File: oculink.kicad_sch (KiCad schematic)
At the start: 14 parts, among them J1 OCuLink_x4_Amphenol_G14A42121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

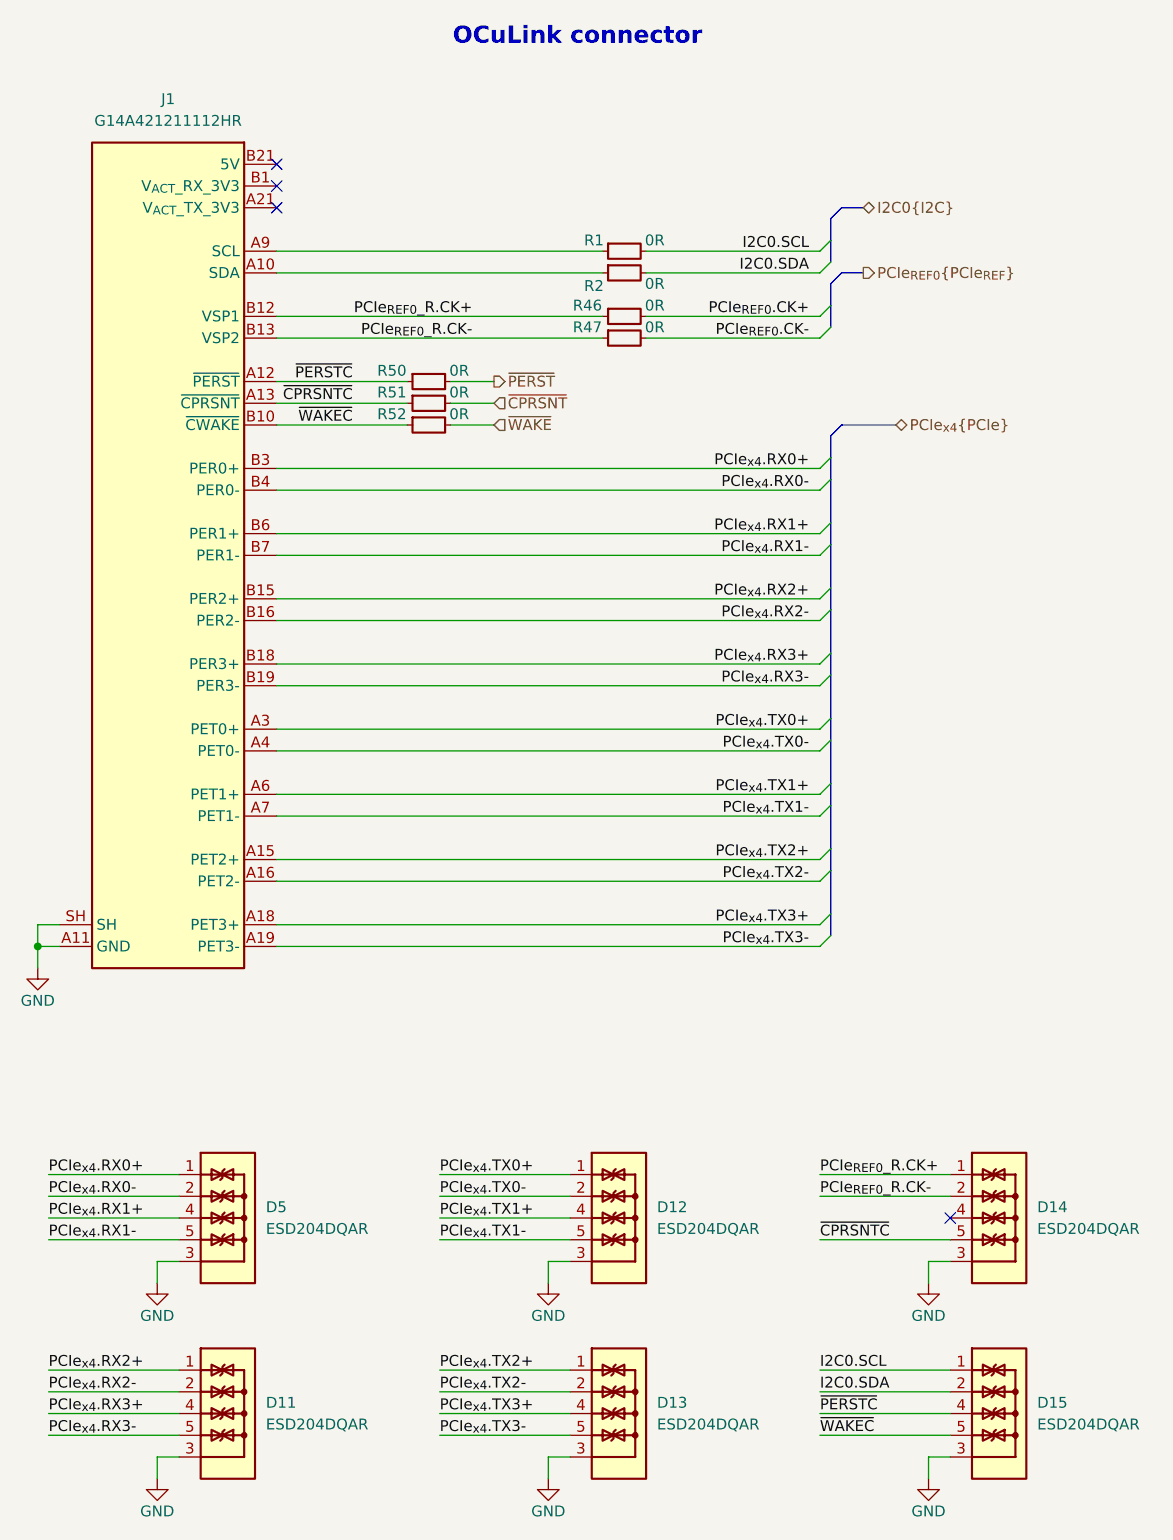
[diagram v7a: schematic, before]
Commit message: [#79262] Route high speed and power
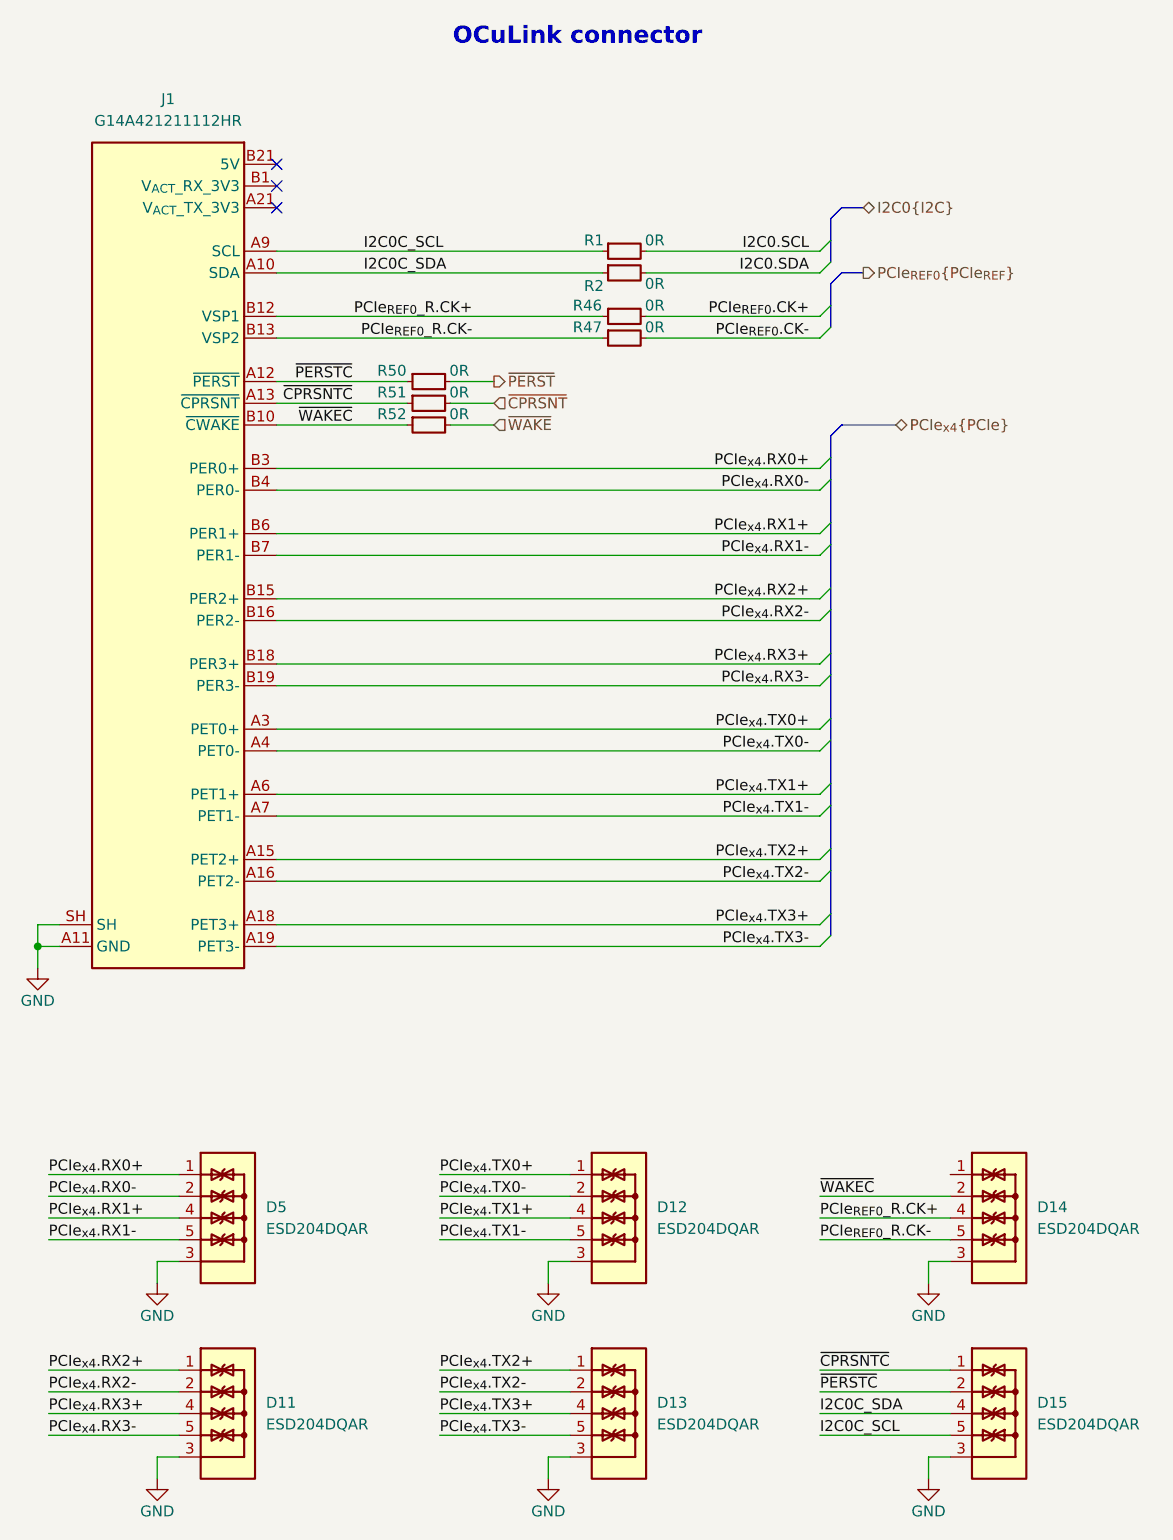
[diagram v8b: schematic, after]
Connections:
- net I2C0.SCL: no longer D15.1, D15.10
- net I2C0.SDA: no longer D15.2, D15.9
- net PCIe_{REF0}_R.CK+: now also D14.4, D14.7; no longer D14.1, D14.10
- net PCIe_{REF0}_R.CK-: now also D14.5, D14.6; no longer D14.2, D14.9
- net ~{CPRSNTC}: now also D15.1, D15.10; no longer D14.5, D14.6
- net ~{PERSTC}: now also D15.2, D15.9; no longer D15.4, D15.7
- net ~{WAKEC}: now also D14.2, D14.9; no longer D15.5, D15.6
- net I2C0C_SDA: now reaches J1.A10 (SDA), R2.1
- net I2C0C_SDA: now also D15.4, D15.7
- net I2C0C_SCL: now reaches J1.A9 (SCL), R1.1
- net I2C0C_SCL: now also D15.5, D15.6
- new net: D14.1, D14.10
- no-connect marks 4 -> 3
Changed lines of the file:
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@@
-	)
-	(no_connect
-		(at 246.38 215.9)
 	)
 	(no_connect
@@
 	(wire
 		(pts
+			(xy 231.14 213.36) (xy 246.38 213.36)
+		)
+		(stroke
+			(width 0)
+			(type default)
+		)
+	)
+	(wire
+		(pts
 			(xy 231.14 241.3) (xy 246.38 241.3)
 		)
@@
 	(wire
 		(pts
-			(xy 231.14 210.82) (xy 246.38 210.82)
+			(xy 231.14 215.9) (xy 246.38 215.9)
 		)
 		(stroke
@@
 	(wire
 		(pts
+			(xy 142.24 181.61) (xy 139.7 181.61)
+		)
+		(stroke
+			(width 0)
+			(type default)
+		)
+	)
+	(wire
+		(pts
+			(xy 231.14 173.99) (xy 167.64 173.99)
+		)
+		(stroke
+			(width 0)
+			(type default)
+		)
+	)
+	(wire
+		(pts
+			(xy 140.97 238.76) (xy 156.21 238.76)
+		)
+		(stroke
+			(width 0)
+			(type default)
+		)
+	)
+	(bus
+		(pts
+			(xy 232.41 152.4) (xy 232.41 157.48)
+		)
+		(stroke
+			(width 0)
+			(type default)
+		)
+	)
+	(wire
+		(pts
+			(xy 167.64 138.43) (xy 231.14 138.43)
+		)
+		(stroke
+			(width 0)
+			(type default)
+		)
+	)
+	(wire
+		(pts
+			(xy 153.67 220.98) (xy 153.67 223.52)
+		)
+		(stroke
+			(width 0)
+			(type default)
+		)
+	)
+	(wire
+		(pts
+			(xy 167.64 102.87) (xy 205.74 102.87)
+		)
+		(stroke
+			(width 0)
+			(type default)
+		)
+	)
+	(wire
+		(pts
+			(xy 199.39 220.98) (xy 201.93 220.98)
+		)
+		(stroke
+			(width 0)
+			(type default)
+		)
+	)
+	(wire
+		(pts
+			(xy 210.82 102.87) (xy 231.14 102.87)
+		)
+		(stroke
+			(width 0)
+			(type default)
+		)
+	)
+	(wire
+		(pts
 			(xy 231.14 218.44) (xy 246.38 218.44)
-		)
-		(stroke
-			(width 0)
-			(type default)
-		)
-	)
-	(wire
-		(pts
-			(xy 142.24 181.61) (xy 139.7 181.61)
-		)
-		(stroke
-			(width 0)
-			(type default)
-		)
-	)
-	(wire
-		(pts
-			(xy 231.14 173.99) (xy 167.64 173.99)
-		)
-		(stroke
-			(width 0)
-			(type default)
-		)
-	)
-	(wire
-		(pts
-			(xy 140.97 238.76) (xy 156.21 238.76)
-		)
-		(stroke
-			(width 0)
-			(type default)
-		)
-	)
-	(bus
-		(pts
-			(xy 232.41 152.4) (xy 232.41 157.48)
-		)
-		(stroke
-			(width 0)
-			(type default)
-		)
-	)
-	(wire
-		(pts
-			(xy 167.64 138.43) (xy 231.14 138.43)
-		)
-		(stroke
-			(width 0)
-			(type default)
-		)
-	)
-	(wire
-		(pts
-			(xy 153.67 220.98) (xy 153.67 223.52)
-		)
-		(stroke
-			(width 0)
-			(type default)
-		)
-	)
-	(wire
-		(pts
-			(xy 167.64 102.87) (xy 205.74 102.87)
-		)
-		(stroke
-			(width 0)
-			(type default)
-		)
-	)
-	(wire
-		(pts
-			(xy 199.39 220.98) (xy 201.93 220.98)
-		)
-		(stroke
-			(width 0)
-			(type default)
-		)
-	)
-	(wire
-		(pts
-			(xy 210.82 102.87) (xy 231.14 102.87)
-		)
-		(stroke
-			(width 0)
-			(type default)
-		)
-	)
-	(wire
-		(pts
-			(xy 231.14 213.36) (xy 246.38 213.36)
 		)
 		(stroke
@@
 	)
 	(label "~{CPRSNTC}"
-		(at 231.14 218.44 0)
+		(at 231.14 233.68 0)
 		(effects
 			(font
@@
 		)
 	)
-	(label "I2C0.SCL"
-		(at 231.14 233.68 0)
-		(effects
-			(font
-				(size 1.27 1.27)
-			)
-			(justify left bottom)
-		)
-	)
 	(label "PCIe_{REF0}_R.CK+"
 		(at 190.5 110.49 180)
@@
 		)
 	)
+	(label "I2C0C_SDA"
+		(at 231.14 238.76 0)
+		(effects
+			(font
+				(size 1.27 1.27)
+			)
+			(justify left bottom)
+		)
+	)
 	(label "PCIe_{x4}.RX1-"
 		(at 229.87 138.43 180)
@@
 		)
 	)
-	(label "~{WAKEC}"
-		(at 231.14 241.3 0)
-		(effects
-			(font
-				(size 1.27 1.27)
-			)
-			(justify left bottom)
-		)
-	)
 	(label "PCIe_{REF0}_R.CK+"
-		(at 231.14 210.82 0)
+		(at 231.14 215.9 0)
 		(effects
 			(font
@@
 	)
 	(label "~{PERSTC}"
-		(at 231.14 238.76 0)
+		(at 231.14 236.22 0)
 		(effects
 			(font
@@
 		)
 	)
-	(label "I2C0.SDA"
-		(at 231.14 236.22 0)
+	(label "I2C0C_SCL"
+		(at 177.8 102.87 0)
 		(effects
 			(font
@@
 		)
 	)
+	(label "I2C0C_SDA"
+		(at 177.8 105.41 0)
+		(effects
+			(font
+				(size 1.27 1.27)
+			)
+			(justify left bottom)
+		)
+	)
 	(label "PCIe_{REF0}_R.CK-"
-		(at 231.14 213.36 0)
+		(at 231.14 218.44 0)
 		(effects
 			(font
@@
 		)
 	)
+	(label "I2C0C_SCL"
+		(at 231.14 241.3 0)
+		(effects
+			(font
+				(size 1.27 1.27)
+			)
+			(justify left bottom)
+		)
+	)
 	(label "PCIe_{x4}.TX1-"
 		(at 186.69 218.44 0)
 		(effects
 			(font
+				(size 1.27 1.27)
+			)
+			(justify left bottom)
+		)
+	)
+	(label "~{WAKEC}"
+		(at 231.14 213.36 0)
+		(effects
+			(font
